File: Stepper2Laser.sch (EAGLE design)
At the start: 7 parts

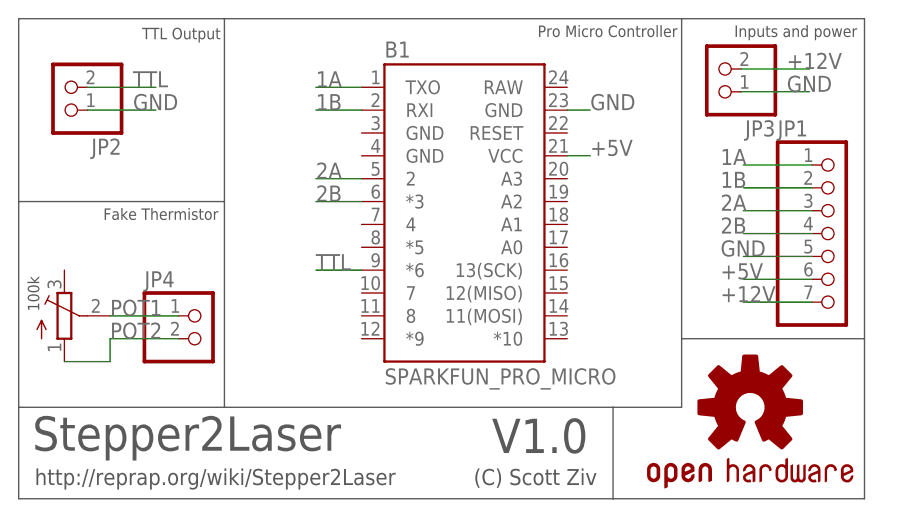
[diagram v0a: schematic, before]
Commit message: Added first firmware version, fixed some trace issues.
Added firmware and minor fixes. Still in development, and relies on
retraction to work.
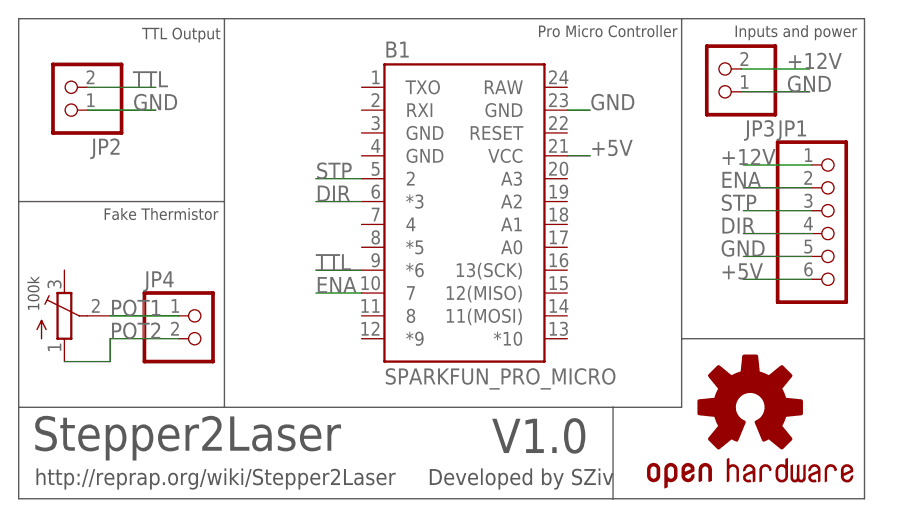
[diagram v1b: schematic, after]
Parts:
- JP1: device pinhead:PINHD-1X7 -> adafruit:PINHD-1X6
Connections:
- net 2A renamed STP
- net 2B renamed DIR
- removed net 1A: B1.TXO, JP1.1
- removed net 1B: B1.RXI, JP1.2
- new net ENA: B1.7, JP1.2
- net +12V: now also JP1.1; no longer JP1.7
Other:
- note added: "Developed by SZiv"
- note removed: "(C) Scott Ziv"
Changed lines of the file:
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@@
 <layer number="19" name="Unrouted" color="6" fill="1" visible="no" active="no"/>
 <layer number="20" name="Dimension" color="15" fill="1" visible="no" active="no"/>
-<layer number="21" name="tPlace" color="16" fill="1" visible="no" active="no"/>
-<layer number="22" name="bPlace" color="14" fill="1" visible="no" active="no"/>
+<layer number="21" name="tPlace" color="7" fill="1" visible="no" active="no"/>
+<layer number="22" name="bPlace" color="7" fill="1" visible="no" active="no"/>
 <layer number="23" name="tOrigins" color="15" fill="1" visible="no" active="no"/>
 <layer number="24" name="bOrigins" color="15" fill="1" visible="no" active="no"/>
@@
 <parts>
 <part name="B1" library="SparkFun-Boards" deviceset="SPARKFUN_PRO_MICRO" device=""/>
-<part name="JP1" library="pinhead" library_urn="urn:adsk.eagle:library:325" deviceset="PINHD-1X7" device=""/>
+<part name="JP1" library="adafruit" deviceset="PINHD-1X6" device=""/>
 <part name="JP2" library="pinhead" library_urn="urn:adsk.eagle:library:325" deviceset="PINHD-1X2" device=""/>
 <part name="JP3" library="pinhead" library_urn="urn:adsk.eagle:library:325" deviceset="PINHD-1X2" device=""/>
@@
 <wire x1="83.82" y1="38.1" x2="104.14" y2="38.1" width="0.1524" layer="97"/>
 <wire x1="76.2" y1="30.48" x2="76.2" y2="20.32" width="0.1524" layer="97"/>
-<text x="60.706" y="21.844" size="1.778" layer="97">(C) Scott Ziv</text>
+<text x="55.626" y="21.844" size="1.778" layer="97">Developed by SZiv</text>
 <text x="11.938" y="21.844" size="1.778" layer="97">http://reprap.org/wiki/Stepper2Laser</text>
 <text x="11.684" y="25.654" size="3.81" layer="97">Stepper2Laser</text>
@@
 </segment>
 <segment>
-<pinref part="JP1" gate="A" pin="7"/>
-<wire x1="98.298" y1="42.164" x2="90.678" y2="42.164" width="0.1524" layer="91"/>
-<label x="88.138" y="42.164" size="1.778" layer="95"/>
+<pinref part="JP1" gate="A" pin="1"/>
+<wire x1="98.298" y1="57.404" x2="90.678" y2="57.404" width="0.1524" layer="91"/>
+<label x="88.138" y="57.404" size="1.778" layer="95"/>
 </segment>
 </net>
@@
 <wire x1="48.26" y1="45.72" x2="43.18" y2="45.72" width="0.1524" layer="91"/>
 <label x="43.18" y="45.72" size="1.778" layer="95"/>
-</segment>
-</net>
-<net name="2B" class="0">
-<segment>
-<pinref part="JP1" gate="A" pin="4"/>
-<wire x1="98.298" y1="49.784" x2="90.678" y2="49.784" width="0.1524" layer="91"/>
-<label x="88.138" y="49.784" size="1.778" layer="95"/>
-</segment>
-<segment>
-<pinref part="B1" gate="G$1" pin="*3"/>
-<wire x1="48.26" y1="53.34" x2="43.18" y2="53.34" width="0.1524" layer="91"/>
-<label x="43.18" y="53.34" size="1.778" layer="95"/>
-</segment>
-</net>
-<net name="2A" class="0">
-<segment>
-<pinref part="JP1" gate="A" pin="3"/>
-<wire x1="98.298" y1="52.324" x2="90.678" y2="52.324" width="0.1524" layer="91"/>
-<label x="88.138" y="52.324" size="1.778" layer="95"/>
-</segment>
-<segment>
-<pinref part="B1" gate="G$1" pin="2"/>
-<wire x1="48.26" y1="55.88" x2="43.18" y2="55.88" width="0.1524" layer="91"/>
-<label x="43.18" y="55.88" size="1.778" layer="95"/>
-</segment>
-</net>
-<net name="1B" class="0">
-<segment>
-<pinref part="JP1" gate="A" pin="2"/>
-<wire x1="98.298" y1="54.864" x2="90.678" y2="54.864" width="0.1524" layer="91"/>
-<label x="88.138" y="54.864" size="1.778" layer="95"/>
-</segment>
-<segment>
-<pinref part="B1" gate="G$1" pin="RXI"/>
-<wire x1="48.26" y1="63.5" x2="43.18" y2="63.5" width="0.1524" layer="91"/>
-<label x="43.18" y="63.5" size="1.778" layer="95"/>
-</segment>
-</net>
-<net name="1A" class="0">
-<segment>
-<pinref part="JP1" gate="A" pin="1"/>
-<wire x1="98.298" y1="57.404" x2="90.678" y2="57.404" width="0.1524" layer="91"/>
-<label x="88.138" y="57.404" size="1.778" layer="95"/>
-</segment>
-<segment>
-<pinref part="B1" gate="G$1" pin="TXO"/>
-<wire x1="48.26" y1="66.04" x2="43.18" y2="66.04" width="0.1524" layer="91"/>
-<label x="43.18" y="66.04" size="1.778" layer="95"/>
 </segment>
 </net>
@@
 </segment>
 </net>
+<net name="DIR" class="0">
+<segment>
+<pinref part="JP1" gate="A" pin="4"/>
+<wire x1="98.298" y1="49.784" x2="90.678" y2="49.784" width="0.1524" layer="91"/>
+<label x="88.138" y="49.784" size="1.778" layer="95"/>
+</segment>
+<segment>
+<pinref part="B1" gate="G$1" pin="*3"/>
+<wire x1="48.26" y1="53.34" x2="43.18" y2="53.34" width="0.1524" layer="91"/>
+<label x="43.18" y="53.34" size="1.778" layer="95"/>
+</segment>
+</net>
+<net name="STP" class="0">
+<segment>
+<pinref part="JP1" gate="A" pin="3"/>
+<wire x1="98.298" y1="52.324" x2="90.678" y2="52.324" width="0.1524" layer="91"/>
+<label x="88.138" y="52.324" size="1.778" layer="95"/>
+</segment>
+<segment>
+<pinref part="B1" gate="G$1" pin="2"/>
+<wire x1="48.26" y1="55.88" x2="43.18" y2="55.88" width="0.1524" layer="91"/>
+<label x="43.18" y="55.88" size="1.778" layer="95"/>
+</segment>
+</net>
+<net name="ENA" class="0">
+<segment>
+<pinref part="JP1" gate="A" pin="2"/>
+<wire x1="98.298" y1="54.864" x2="90.678" y2="54.864" width="0.1524" layer="91"/>
+<label x="88.138" y="54.864" size="1.778" layer="95"/>
+</segment>
+<segment>
+<pinref part="B1" gate="G$1" pin="7"/>
+<wire x1="48.26" y1="43.18" x2="43.18" y2="43.18" width="0.1524" layer="91"/>
+<label x="43.18" y="43.18" size="1.778" layer="95"/>
+</segment>
+</net>
